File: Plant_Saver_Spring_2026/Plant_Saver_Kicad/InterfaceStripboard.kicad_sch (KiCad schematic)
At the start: 14 parts, among them SW17 Select, SW18 3-1825910-5, SW19 3-1825910-5, SW20 3-1825910-5, SW3 3-1825910-5, SW4 Up, SW5 Down, SW6 Change Screen

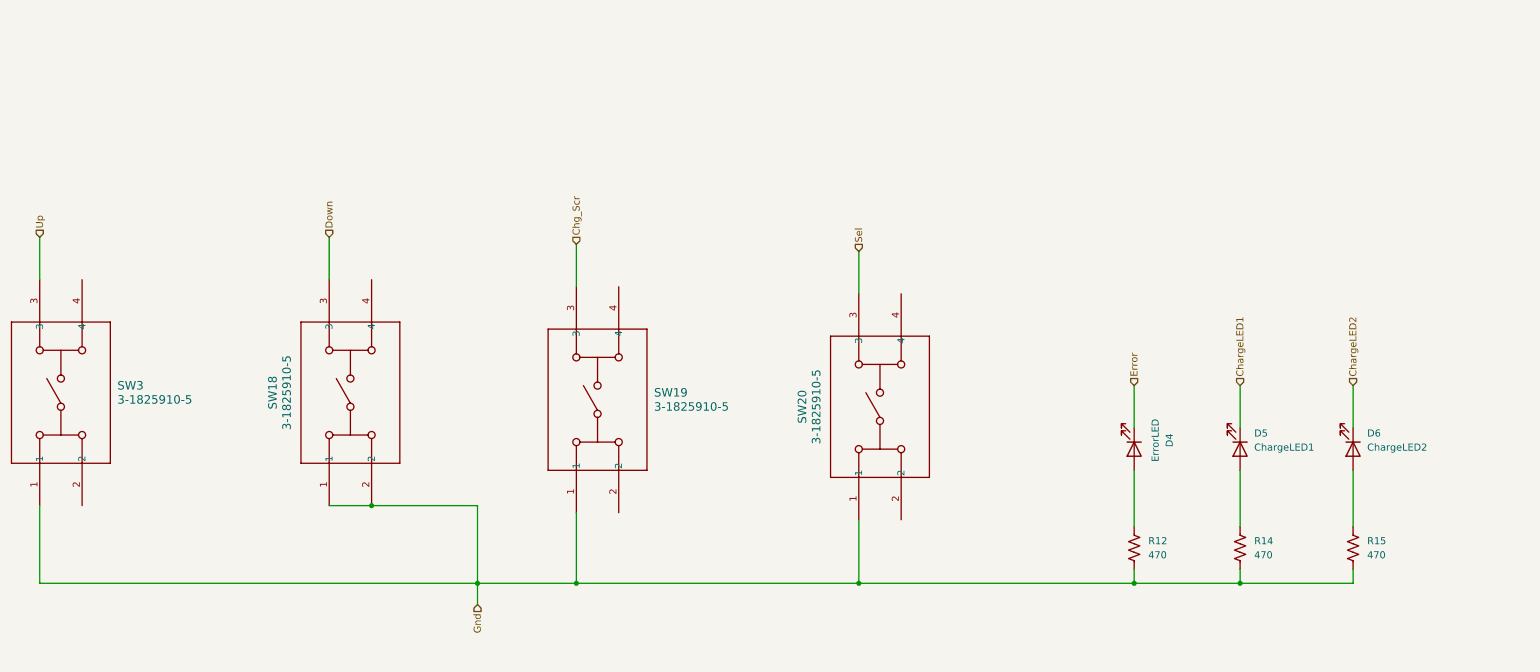
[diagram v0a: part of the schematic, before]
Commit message: StripBoardTouchUp
Made everything on the stripboard go into connector pins that then integrate into the main sketch. Made Error LED go into pin 26 on the esp32.
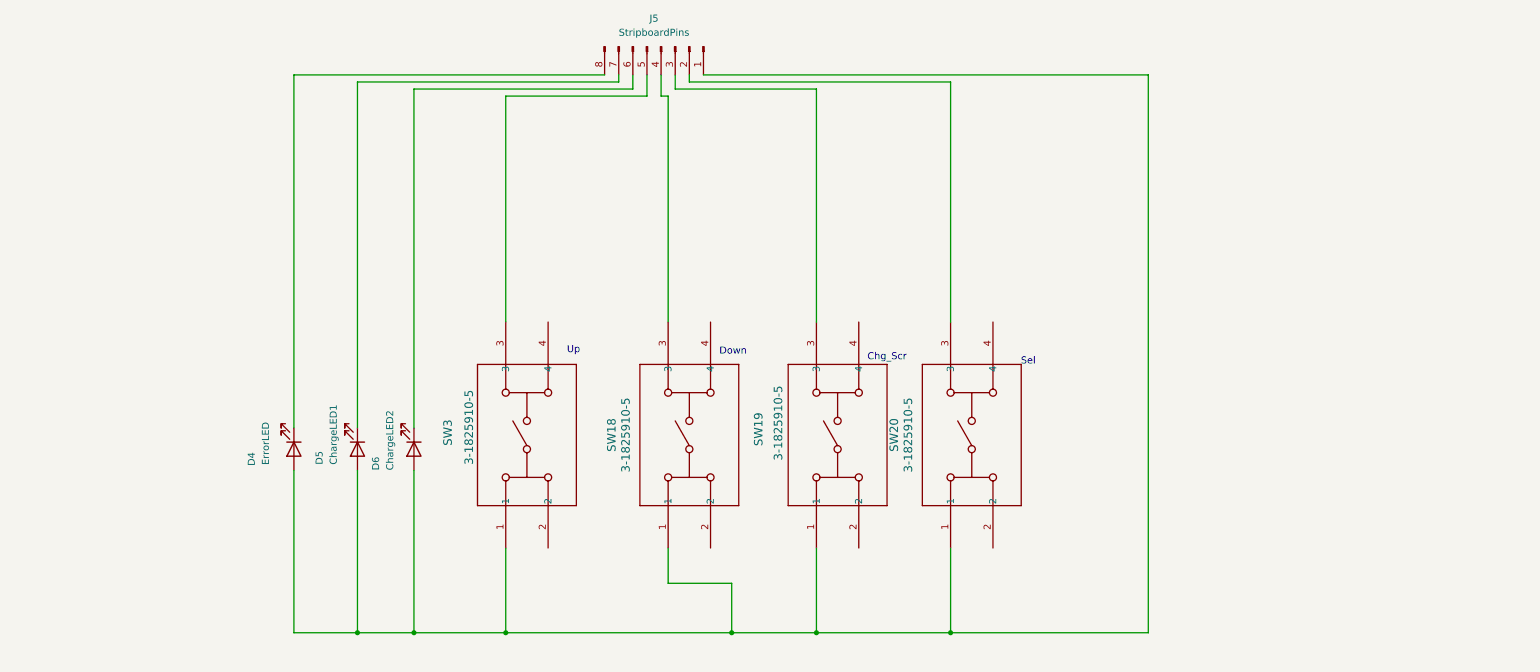
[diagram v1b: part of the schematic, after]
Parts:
- removed R12, R14, R15: 470, symbol Device:R_US
- added J5: StripboardPins, symbol Connector:Conn_01x08_Pin
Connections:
- net Chg_Scr: no longer SW19.3
- net Down: no longer SW18.3
- net Gnd: no longer SW18.1, SW18.2, SW19.1, SW20.1, SW3.1
- net Sel: no longer SW20.3
- net Up: no longer SW3.3
- net at D4.2 (A): now also D5.2 (A), D6.2 (A), SW18.1, SW19.1, SW20.1, SW3.1, J5.1 (Pin_1)
- net ChargeLED1: no longer names the net of D5.1 (K)
- net ChargeLED1: now also J5.7 (Pin_7)
- net ChargeLED2: no longer names the net of D6.1 (K)
- net ChargeLED2: now also J5.6 (Pin_6)
- net Error: no longer names the net of D4.1 (K)
- net Error: now also J5.8 (Pin_8)
- new net: J5.5 (Pin_5), SW3.3
- new net: J5.4 (Pin_4), SW18.3
- new net: J5.3 (Pin_3), SW19.3
- new net: J5.2 (Pin_2), SW20.3
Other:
- note added: "Chg_Scr"
- note added: "Down"
- note added: "Sel"
- note added: "Up"
- moved on the sheet: D4, D5, D6, SW18, SW19, SW20, SW3

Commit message: Misc. changes
Updated peripheral power switch, UI board connections
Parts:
- removed SW17: Select, symbol Switch:SW_Push
- removed SW4: Up, symbol Switch:SW_Push
- removed SW5: Down, symbol Switch:SW_Push
- removed SW6: Change Screen, symbol Switch:SW_Push
- added SW10: Down, 3_1825910_5:SW4_1825910-I_TEC, symbol Switch:SW_Push
- added SW11: Change Screen, 3_1825910_5:SW4_1825910-I_TEC, symbol Switch:SW_Push
- added SW12: Select, 3_1825910_5:SW4_1825910-I_TEC, symbol Switch:SW_Push
- added SW9: Up, 3_1825910_5:SW4_1825910-I_TEC, symbol Switch:SW_Push
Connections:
- net at J5.1 (Pin_1), SW18.1, SW19.1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: no longer D4.2 (A), D5.2 (A), D6.2 (A)
- net at J5.8 (Pin_8): no longer D4.1 (K)
- net at J5.6 (Pin_6): no longer D6.1 (K)
- net at J5.7 (Pin_7): no longer D5.1 (K)
- new net Chg_Cpt_Lt: D6.2 (A)
- new net Chg_Lt: D5.2 (A)
- new net Chg_Scr_Btn: SW11.1
- new net Down_Btn: SW10.1
- new net Error_Lt: D4.2 (A)
- new net GND: D4.1 (K), D5.1 (K), D6.1 (K), SW10.2, SW11.2, SW12.2, SW9.2
- new net Sel_Btn: SW12.1
- new net Up_Btn: SW9.1
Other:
- note added: "**NOTE** Internal pullups used for interface buttons"
- note removed: "Interface Buttons"
- moved on the sheet: D4, D5, D6, J5, SW18, SW19, SW20, SW3

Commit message: Misc. fixes to schematic
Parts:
- removed J5: StripboardPins, symbol Connector:Conn_01x08_Pin
- removed SW18, SW19, SW20, SW3: 3-1825910-5, SW4_1825910-I_TEC, symbol 2026-02-06_15-15-45:3-1825910-5
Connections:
- net Chg_Cpt_Lt: now also D6.1 (K); no longer D6.2 (A)
- net Chg_Lt: now also D5.1 (K); no longer D5.2 (A)
- net GND: no longer D5.1 (K), D6.1 (K)
- new net 3V3: D5.2 (A), D6.2 (A)
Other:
- note removed: "Chg_Scr"
- note removed: "Down"
- note removed: "Sel"
- note removed: "Up"
- moved on the sheet: D4, D5, D6, SW10, SW11, SW12, SW9

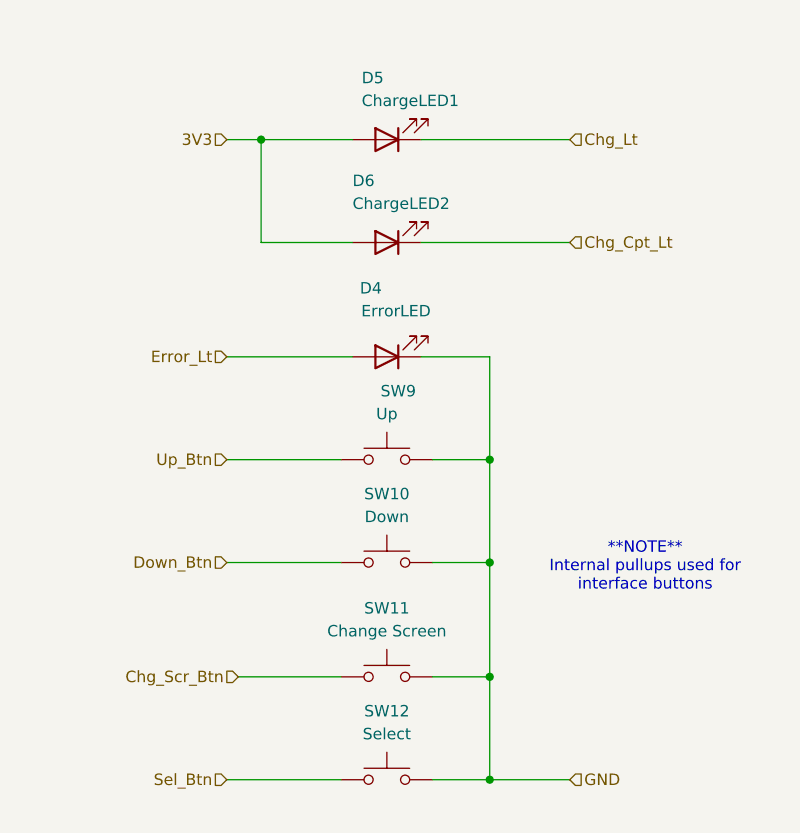
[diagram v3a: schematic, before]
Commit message: Footprint updates
Misc. schematic fixes, mostly updated/added footprints where needed.
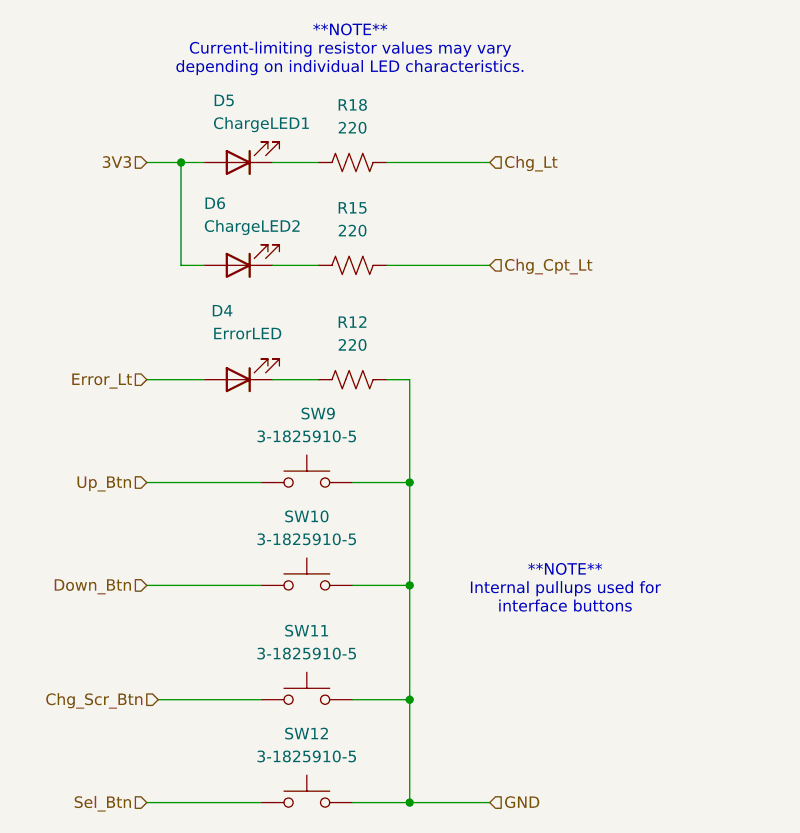
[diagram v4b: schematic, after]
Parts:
- added R12, R15, R18: 220, Resistor_THT:R_Axial_DIN0207_L6.3mm_D2.5mm_P10.16mm_Horizontal, symbol Device:R_US
- SW10: value Down -> 3-1825910-5
- SW11: value Change Screen -> 3-1825910-5
- SW12: value Select -> 3-1825910-5
- SW9: value Up -> 3-1825910-5
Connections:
- net Chg_Cpt_Lt: now also R15.2; no longer D6.1 (K)
- net Chg_Lt: now also R18.2; no longer D5.1 (K)
- net GND: now also R12.2; no longer D4.1 (K)
- new net: D6.1 (K), R15.1
- new net: D4.1 (K), R12.1
- new net: D5.1 (K), R18.1
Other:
- note added: "**NOTE** Current-limiting resistor values may vary depending on individual LED characteristics."
- moved on the sheet: D4, D5, D6, SW10, SW11, SW12, SW9

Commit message: Started PCB
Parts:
- renumbered D5 to D1, D6 to D2, D4 to D3, R18 to R25, R15 to R26, R12 to R27, SW9 to SW5, SW10 to SW6, SW11 to SW7, SW12 to SW8
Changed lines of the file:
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@@
 		(dnp no)
 		(fields_autoplaced yes)
-		(property "Reference" "R15"
+		(property "Reference" "R26"
 			(at 149.86 66.04 90)
 			(effects
@@
 			(project "Plant_Saver_Kicad"
 				(path "/7f244634-d37a-4ff0-ba36-8027330ab1bd/dee11cd4-4b8f-4bcd-86fc-bdb1a9aa17df"
-					(reference "R15")
+					(reference "R26")
 					(unit 1)
 				)
@@
 		(dnp no)
 		(fields_autoplaced yes)
-		(property "Reference" "R12"
+		(property "Reference" "R27"
 			(at 149.86 78.74 90)
 			(effects
@@
 			(project "Plant_Saver_Kicad"
 				(path "/7f244634-d37a-4ff0-ba36-8027330ab1bd/dee11cd4-4b8f-4bcd-86fc-bdb1a9aa17df"
-					(reference "R12")
+					(reference "R27")
 					(unit 1)
 				)
@@
 		(dnp no)
 		(fields_autoplaced yes)
-		(property "Reference" "SW11"
+		(property "Reference" "SW7"
 			(at 144.78 113.03 0)
 			(effects
@@
 			(project "Plant_Saver_Kicad"
 				(path "/7f244634-d37a-4ff0-ba36-8027330ab1bd/dee11cd4-4b8f-4bcd-86fc-bdb1a9aa17df"
-					(reference "SW11")
+					(reference "SW7")
 					(unit 1)
 				)
@@
 		(on_board yes)
 		(dnp no)
-		(property "Reference" "D4"
+		(property "Reference" "D3"
 			(at 135.382 77.47 0)
 			(effects
@@
 			(project "Plant_Saver_Kicad"
 				(path "/7f244634-d37a-4ff0-ba36-8027330ab1bd/dee11cd4-4b8f-4bcd-86fc-bdb1a9aa17df"
-					(reference "D4")
+					(reference "D3")
 					(unit 1)
 				)
@@
 		(dnp no)
 		(fields_autoplaced yes)
-		(property "Reference" "SW12"
+		(property "Reference" "SW8"
 			(at 144.78 124.46 0)
 			(effects
@@
 			(project "Plant_Saver_Kicad"
 				(path "/7f244634-d37a-4ff0-ba36-8027330ab1bd/dee11cd4-4b8f-4bcd-86fc-bdb1a9aa17df"
-					(reference "SW12")
+					(reference "SW8")
 					(unit 1)
 				)
@@
 		(dnp no)
 		(fields_autoplaced yes)
-		(property "Reference" "SW10"
+		(property "Reference" "SW6"
 			(at 144.78 100.33 0)
 			(effects
@@
 			(project "Plant_Saver_Kicad"
 				(path "/7f244634-d37a-4ff0-ba36-8027330ab1bd/dee11cd4-4b8f-4bcd-86fc-bdb1a9aa17df"
-					(reference "SW10")
+					(reference "SW6")
 					(unit 1)
 				)
@@
 		(on_board yes)
 		(dnp no)
-		(property "Reference" "SW9"
+		(property "Reference" "SW5"
 			(at 146.05 88.9 0)
 			(effects
@@
 			(project ""
 				(path "/7f244634-d37a-4ff0-ba36-8027330ab1bd/dee11cd4-4b8f-4bcd-86fc-bdb1a9aa17df"
-					(reference "SW9")
+					(reference "SW5")
 					(unit 1)
 				)
@@
 		(on_board yes)
 		(dnp no)
-		(property "Reference" "D5"
+		(property "Reference" "D1"
 			(at 134.366 54.102 0)
 			(effects
@@
 			(project "Plant_Saver_Kicad"
 				(path "/7f244634-d37a-4ff0-ba36-8027330ab1bd/dee11cd4-4b8f-4bcd-86fc-bdb1a9aa17df"
-					(reference "D5")
+					(reference "D1")
 					(unit 1)
 				)
@@
 		(dnp no)
 		(fields_autoplaced yes)
-		(property "Reference" "R18"
+		(property "Reference" "R25"
 			(at 149.86 54.61 90)
 			(effects
@@
 			(project "Plant_Saver_Kicad"
 				(path "/7f244634-d37a-4ff0-ba36-8027330ab1bd/dee11cd4-4b8f-4bcd-86fc-bdb1a9aa17df"
-					(reference "R18")
+					(reference "R25")
 					(unit 1)
 				)
@@
 		(on_board yes)
 		(dnp no)
-		(property "Reference" "D6"
+		(property "Reference" "D2"
 			(at 133.35 65.532 0)
 			(effects
@@
 			(project "Plant_Saver_Kicad"
 				(path "/7f244634-d37a-4ff0-ba36-8027330ab1bd/dee11cd4-4b8f-4bcd-86fc-bdb1a9aa17df"
-					(reference "D6")
-					(unit 1)
-				)
+					(reference "D2")
+					(unit 1)
+				)

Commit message: PCB Pre-Check complete
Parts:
- renumbered R25 to R27, R26 to R28, R27 to R29
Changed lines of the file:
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@@
 		(dnp no)
 		(fields_autoplaced yes)
-		(property "Reference" "R26"
+		(property "Reference" "R28"
 			(at 149.86 66.04 90)
 			(effects
@@
 			(project "Plant_Saver_Kicad"
 				(path "/7f244634-d37a-4ff0-ba36-8027330ab1bd/dee11cd4-4b8f-4bcd-86fc-bdb1a9aa17df"
-					(reference "R26")
+					(reference "R28")
 					(unit 1)
 				)
@@
 		(dnp no)
 		(fields_autoplaced yes)
-		(property "Reference" "R27"
+		(property "Reference" "R29"
 			(at 149.86 78.74 90)
 			(effects
@@
 			(project "Plant_Saver_Kicad"
 				(path "/7f244634-d37a-4ff0-ba36-8027330ab1bd/dee11cd4-4b8f-4bcd-86fc-bdb1a9aa17df"
-					(reference "R27")
+					(reference "R29")
 					(unit 1)
 				)
@@
 		(dnp no)
 		(fields_autoplaced yes)
-		(property "Reference" "R25"
+		(property "Reference" "R27"
 			(at 149.86 54.61 90)
 			(effects
@@
 			(project "Plant_Saver_Kicad"
 				(path "/7f244634-d37a-4ff0-ba36-8027330ab1bd/dee11cd4-4b8f-4bcd-86fc-bdb1a9aa17df"
-					(reference "R25")
-					(unit 1)
-				)
+					(reference "R27")
+					(unit 1)
+				)
